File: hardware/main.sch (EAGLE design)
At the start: 99 parts, among them IC1 MPU-6050, IC2 TB6612FNG, M1 MOTOR_MOUNT_V2, M2 LED_MOUNT, M3 LED_MOUNT, M4 LED_MOUNT, M5 LED_MOUNT, M6 LED_MOUNT, M7 LED_MOUNT, Q7 IRLML2244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

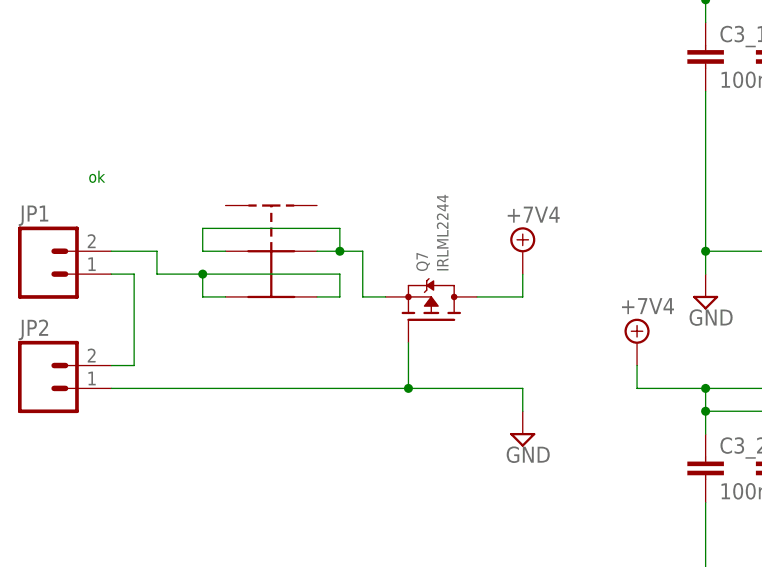
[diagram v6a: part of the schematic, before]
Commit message: bugfix: mosfet przy zasilaniu
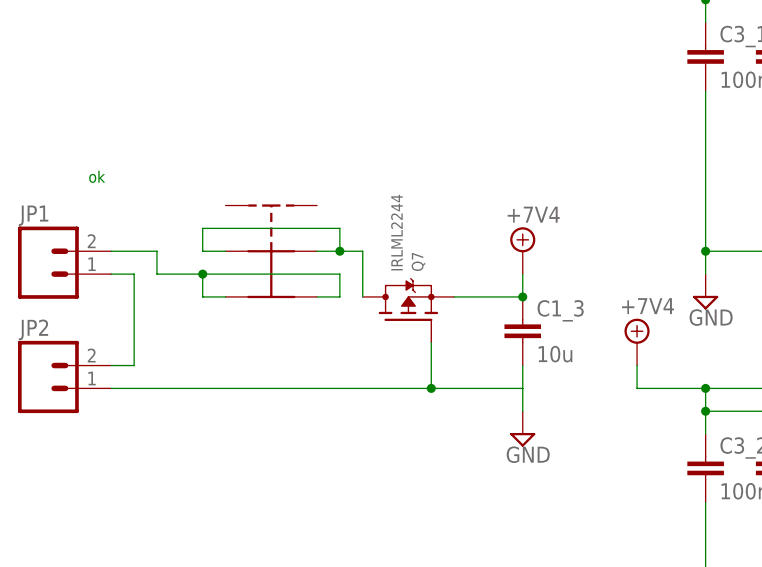
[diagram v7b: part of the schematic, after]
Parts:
- added C1_3: 10u, rcl:C-EUC0805
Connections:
- net +7V: now also C1_3.1, Q7.S; no longer Q7.D
- net GND: now also C1_3.2
- net N$43: now also Q7.D; no longer Q7.S
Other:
- moved on the sheet: Q7
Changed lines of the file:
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@@
 <part name="AGND1" library="supply2" deviceset="GND" device=""/>
 <part name="+3V28" library="supply1" deviceset="+3V3" device=""/>
+<part name="C1_3" library="rcl" deviceset="C-EU" device="C0805" value="10u"/>
 </parts>
 <sheets>
@@
 <instance part="C7" gate="G$1" x="86.36" y="335.28" rot="R180"/>
 <instance part="GND1" gate="1" x="86.36" y="325.12"/>
-<instance part="Q7" gate="G$1" x="-154.94" y="142.24" rot="R90"/>
+<instance part="Q7" gate="G$1" x="-157.48" y="142.24" rot="MR90"/>
 <instance part="ON" gate="G$1" x="-172.72" y="147.32" rot="R270"/>
 <instance part="R22" gate="G$1" x="-25.4" y="-15.24" rot="R90"/>
@@
 <instance part="AGND1" gate="GND" x="137.16" y="-20.32"/>
 <instance part="+3V28" gate="G$1" x="137.16" y="5.08"/>
+<instance part="C1_3" gate="G$1" x="-144.78" y="139.7"/>
 </instances>
 <busses>
@@
 <segment>
 <pinref part="Q7" gate="G$1" pin="G"/>
-<wire x1="-157.48" y1="132.08" x2="-157.48" y2="137.16" width="0.1524" layer="91"/>
-<wire x1="-157.48" y1="132.08" x2="-144.78" y2="132.08" width="0.1524" layer="91"/>
+<wire x1="-154.94" y1="132.08" x2="-154.94" y2="137.16" width="0.1524" layer="91"/>
+<wire x1="-154.94" y1="132.08" x2="-144.78" y2="132.08" width="0.1524" layer="91"/>
 <pinref part="AGND33" gate="GND" pin="GND"/>
 <wire x1="-144.78" y1="129.54" x2="-144.78" y2="132.08" width="0.1524" layer="91"/>
-<wire x1="-190.5" y1="132.08" x2="-157.48" y2="132.08" width="0.1524" layer="91"/>
-<junction x="-157.48" y="132.08"/>
+<wire x1="-190.5" y1="132.08" x2="-154.94" y2="132.08" width="0.1524" layer="91"/>
+<junction x="-154.94" y="132.08"/>
 <pinref part="JP2" gate="G$1" pin="1"/>
+<pinref part="C1_3" gate="G$1" pin="2"/>
+<wire x1="-144.78" y1="134.62" x2="-144.78" y2="132.08" width="0.1524" layer="91"/>
 </segment>
 <segment>
@@
 <wire x1="-165.1" y1="147.32" x2="-165.1" y2="149.86" width="0.1524" layer="91"/>
 <wire x1="-165.1" y1="149.86" x2="-180.34" y2="149.86" width="0.1524" layer="91"/>
-<pinref part="Q7" gate="G$1" pin="S"/>
-<wire x1="-160.02" y1="142.24" x2="-162.56" y2="142.24" width="0.1524" layer="91"/>
 <wire x1="-162.56" y1="142.24" x2="-162.56" y2="147.32" width="0.1524" layer="91"/>
 <wire x1="-162.56" y1="147.32" x2="-165.1" y2="147.32" width="0.1524" layer="91"/>
@@
 <wire x1="-177.8" y1="147.32" x2="-180.34" y2="147.32" width="0.1524" layer="91"/>
 <wire x1="-180.34" y1="147.32" x2="-180.34" y2="149.86" width="0.1524" layer="91"/>
+<pinref part="Q7" gate="G$1" pin="D"/>
 </segment>
 </net>
@@
 </segment>
 <segment>
-<pinref part="Q7" gate="G$1" pin="D"/>
-<wire x1="-149.86" y1="142.24" x2="-144.78" y2="142.24" width="0.1524" layer="91"/>
 <pinref part="SUPPLY10" gate="G$1" pin="+7V"/>
 <wire x1="-144.78" y1="142.24" x2="-144.78" y2="144.78" width="0.1524" layer="91"/>
-</segment>
-<segment>
+<pinref part="Q7" gate="G$1" pin="S"/>
+<wire x1="-152.4" y1="142.24" x2="-144.78" y2="142.24" width="0.1524" layer="91"/>
+<pinref part="C1_3" gate="G$1" pin="1"/>
+<junction x="-144.78" y="142.24"/>
+</segment>
+<segment>

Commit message: poukladanie warstwy opisowej, dodanie przelotek - wersja finalna
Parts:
- R26, R27, R28: value 150R -> 300R
- R29: value 33R -> 300R
- R32: value (none) -> 10k
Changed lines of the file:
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@@
 <part name="+3V13" library="supply1" deviceset="+3V3" device=""/>
 <part name="+3V14" library="supply1" deviceset="+3V3" device=""/>
-<part name="R32" library="resistor" deviceset="R-EU_" device="R0603"/>
+<part name="R32" library="resistor" deviceset="R-EU_" device="R0603" value="10k"/>
 <part name="L1_2" library="EAGLE-AECQ_PRODUCTS-rev17b" deviceset="WE-MAIA_3015" device="" technology="_78438335033"/>
 <part name="L1_1" library="EAGLE-AECQ_PRODUCTS-rev17b" deviceset="WE-MAIA_3015" device="" technology="_78438335068"/>
@@
 <part name="S3" library="EAGLE-TACT_SWITCHES-rev17c" deviceset="434153017835" device=""/>
 <part name="S4" library="EAGLE-TACT_SWITCHES-rev17c" deviceset="434153017835" device=""/>
-<part name="R26" library="resistor" deviceset="R-EU_" device="R0603" value="150R"/>
+<part name="R26" library="resistor" deviceset="R-EU_" device="R0603" value="300R"/>
 <part name="+3V15" library="supply1" deviceset="+3V3" device=""/>
 <part name="LED1" library="led" deviceset="LED" device="SML1206" value="red"/>
 <part name="AGND3" library="supply2" deviceset="GND" device=""/>
 <part name="LED2" library="led" deviceset="LED" device="SML1206" value="green"/>
-<part name="R27" library="resistor" deviceset="R-EU_" device="R0603" value="150R"/>
+<part name="R27" library="resistor" deviceset="R-EU_" device="R0603" value="300R"/>
 <part name="+3V18" library="supply1" deviceset="+3V3" device=""/>
-<part name="R28" library="resistor" deviceset="R-EU_" device="R0603" value="150R"/>
+<part name="R28" library="resistor" deviceset="R-EU_" device="R0603" value="300R"/>
 <part name="LED3" library="led" deviceset="LED" device="SML1206" value="yellow"/>
 <part name="+3V19" library="supply1" deviceset="+3V3" device=""/>
 <part name="LED4" library="led" deviceset="LED" device="SML1206" value="blue"/>
-<part name="R29" library="resistor" deviceset="R-EU_" device="R0603" value="33R"/>
+<part name="R29" library="resistor" deviceset="R-EU_" device="R0603" value="300R"/>
 <part name="+3V26" library="supply1" deviceset="+3V3" device=""/>
 <part name="C_V4" library="rcl" deviceset="C-EU" device="C0603" value="100n"/>
